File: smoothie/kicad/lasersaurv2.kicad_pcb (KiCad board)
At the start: 2 copper layers, 32 parts, among them IC1 74LV11, IC2 74HCT08, IC3 AMS1117-3.3, J1 DOOR1, J2 DOOR2, J3 CHILLER, J4 TO_J8, J6 TO_AUX1, J7 LASER_AUX, J8 LASER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

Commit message: More work on PCB.
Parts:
- added C10: 100u, SMD_Packages:SMD-1206_Pol, F.Cu at (147.2, 74.3)
- added C11: 100u, SMD_Packages:SMD-1206_Pol, F.Cu at (207.0, 81.8)
- added D1: D, LEDs:LED_0603, F.Cu at (153.8, 84.6)
- added J10: TO_J7, Connectors:PINHEAD1-6, F.Cu at (239.5, 102.9)
- added J11: 24V PWR, Connectors_JST:JST_PH_B2B-PH-K_02x2.00mm_Straight, F.Cu at (230.1, 78.5)
- added J12: LED LIGHTING, Connectors_JST:JST_PH_B2B-PH-K_02x2.00mm_Straight, F.Cu at (130.6, 102.5)
- added J13: AIR VALVE, Connectors_JST:JST_PH_B2B-PH-K_02x2.00mm_Straight, F.Cu at (136.8, 125.0)
- added J14: AIMING LASER, Connectors_JST:JST_PH_B2B-PH-K_02x2.00mm_Straight, F.Cu at (239.8, 140.0)
- added J5: POWEROFF, Connectors_JST:JST_PH_B3B-PH-K_03x2.00mm_Straight, F.Cu at (124.6, 134.7)
- added Q1: ZXMN4A06, TO_SOT_Packages_SMD:SOT-223-3Lead_TabPin2, F.Cu at (156.3, 73.8)
- added R11: 10K, Resistors_SMD:R_0603, F.Cu at (153.4, 80.4)
- added R12: 22R, Resistors_SMD:R_0603, F.Cu at (158.0, 81.4)
- added U2: DSN-MINI-360, dsn-mini-360:DSN-MINI-360, F.Cu at (217.4, 82.0)
- moved J1 81.8 mm to (101.9, 128.3)
- moved J6 81.6 mm to (240.5, 85.3), turned to 180 degrees
- moved J4 79.5 mm to (239.5, 121.2), turned to 90 degrees
- moved J8 61.8 mm to (232.4, 132.8), turned to 90 degrees
- moved J7 60.2 mm to (226.1, 132.8), turned to 90 degrees
- moved J3 59.4 mm to (142.2, 103.9)
- moved J2 53.6 mm to (239.8, 130.8), turned to 90 degrees
- moved IC2 46.4 mm to (217.9, 130.0), turned to 90 degrees
- moved R9 42.3 mm to (160.5, 132.8)
- moved IC1 35.8 mm to (226.1, 116.1), turned to 90 degrees
- moved R10 30.3 mm to (155.4, 134.6)
- moved R3 30.3 mm to (232.7, 115.3)
- moved R4 29.3 mm to (232.9, 119.9)
- moved R1 24.7 mm to (218.4, 113.0)
- moved R2 19.7 mm to (217.7, 120.4)
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
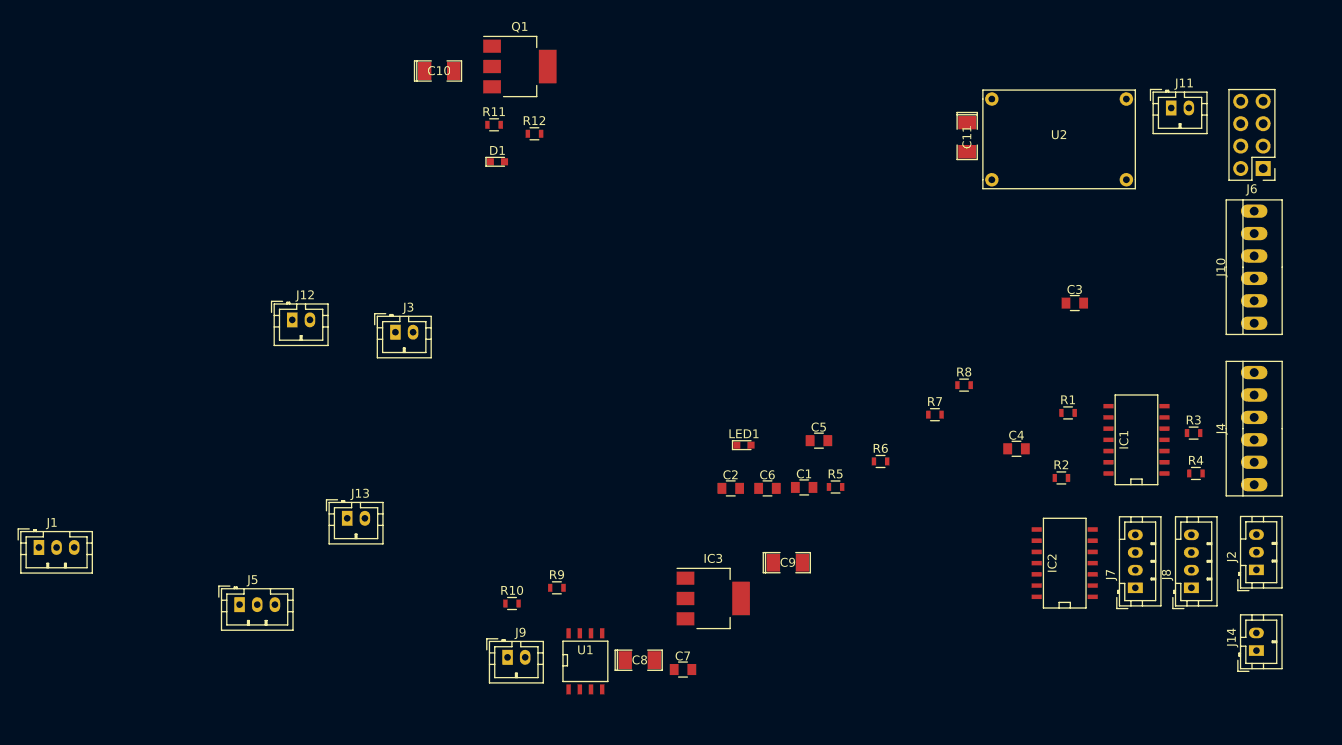
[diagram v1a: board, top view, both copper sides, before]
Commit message: Finish routing.
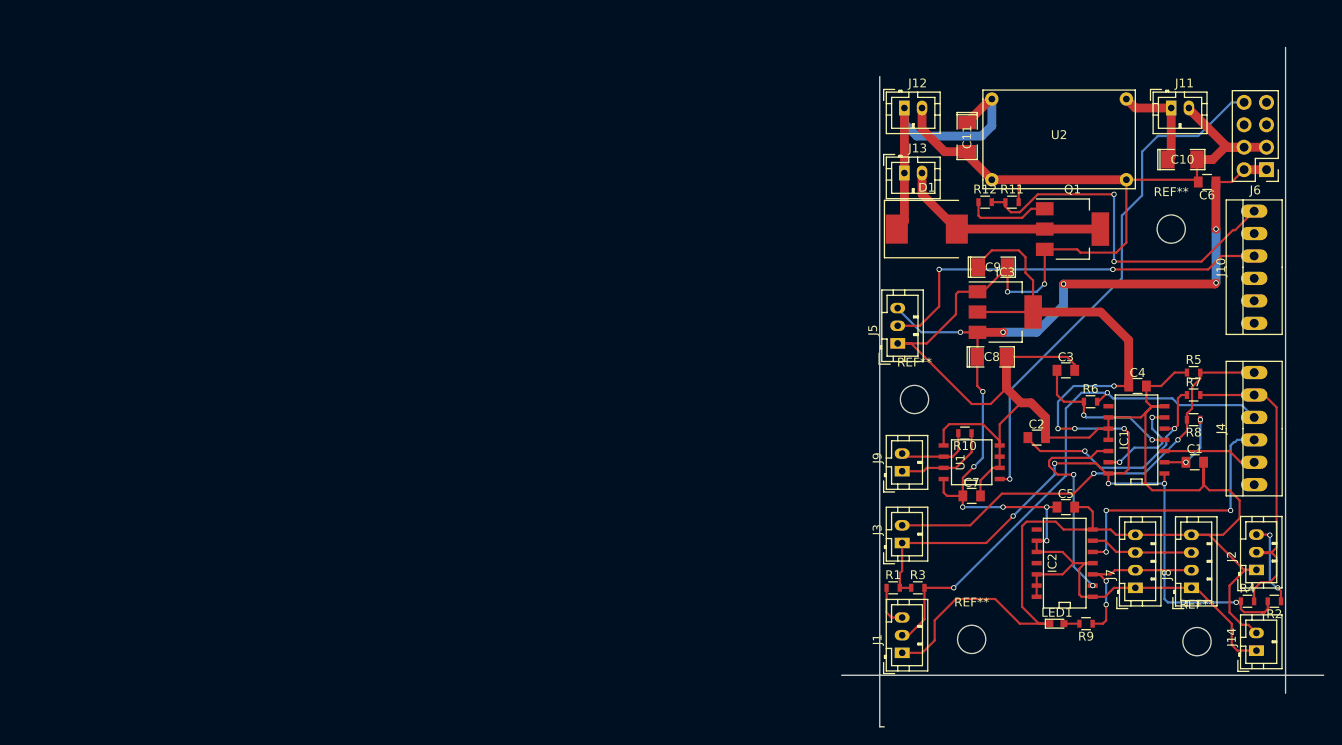
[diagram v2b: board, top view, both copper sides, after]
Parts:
- added REF**: MountingHole_3.2mm_M3, Mounting_Holes:MountingHole_3.2mm_M3, F.Cu at (230.1, 92.2)
- added REF**: MountingHole_3.2mm_M3, Mounting_Holes:MountingHole_3.2mm_M3, F.Cu at (207.5, 138.7)
- added REF**: MountingHole_3.2mm_M3, Mounting_Holes:MountingHole_3.2mm_M3, F.Cu at (201.0, 111.5)
- added REF**: MountingHole_3.2mm_M3, Mounting_Holes:MountingHole_3.2mm_M3, F.Cu at (233.0, 138.9)
- D1: value D -> 1N5822; footprint LEDs:LED_0603 -> Diodes_SMD:D_SMC_Standard
- moved J1 98.5 mm to (199.6, 140.2), turned to 90 degrees
- moved C10 84.8 mm to (231.4, 84.3)
- moved J5 80.2 mm to (199.1, 105.2), turned to 90 degrees
- moved J13 74.3 mm to (199.9, 85.9)
- moved J12 73.4 mm to (199.9, 78.5)
- moved Q1 65.3 mm to (218.9, 92.2)
- moved J3 62.2 mm to (199.6, 127.8), turned to 90 degrees
- moved C6 60.7 mm to (234.2, 86.9), turned to 180 degrees
- moved R9 60.1 mm to (220.5, 136.9), turned to 180 degrees
- moved R11 59.3 mm to (212.1, 89.2)
- moved R10 54.8 mm to (206.8, 115.3), turned to 180 degrees
- moved C8 52.6 mm to (209.8, 106.7)
- moved R12 51.6 mm to (209.0, 89.2)
- moved J9 49.4 mm to (199.6, 119.6), turned to 90 degrees
- moved D1 49.2 mm to (202.4, 92.2)
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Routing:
- net GND: track 0.00 -> 306.7 mm, vias 0 -> 2
- net +5V: track 0.00 -> 144.3 mm, vias 0 -> 11
- net +3V3: track 0.00 -> 134.0 mm, vias 0 -> 9
- net P2.12: track 0.00 -> 60.5 mm, vias 0 -> 2
- net RX: track 0.00 -> 58.3 mm, vias 0 -> 1
- net P4.28: track 0.00 -> 50.4 mm, vias 0 -> 2
- net Net-(J10-Pad4): track 0.00 -> 46.1 mm, vias 0 -> 2
- net Net-(J10-Pad6): track 0.00 -> 41.3 mm, vias 0 -> 2
- net P2.11: track 0.00 -> 36.8 mm
- net Net-(C11-Pad1): track 0.00 -> 33.8 mm
- net P1.23: track 0.00 -> 30.6 mm, vias 0 -> 3
- net Net-(C2-Pad1): track 0.00 -> 26.5 mm, vias 0 -> 2
- net Net-(IC1-Pad12): track 0.00 -> 24.4 mm, vias 0 -> 2
- net Net-(D1-Pad2): track 0.00 -> 24.2 mm
- net Net-(IC2-Pad3): track 0.00 -> 19.4 mm, vias 0 -> 2
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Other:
- board outline added: 54.6 x 77 mm
- net class Power added: clearance 0.2, trace_width 1, via_dia 1, via_drill 0.4

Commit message: Adjust labels.
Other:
- board size 54.6 x 77 mm -> 46 x 66.5 mm
